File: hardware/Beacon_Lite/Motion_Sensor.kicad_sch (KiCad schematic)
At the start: 2 parts, among them U6 BMA530

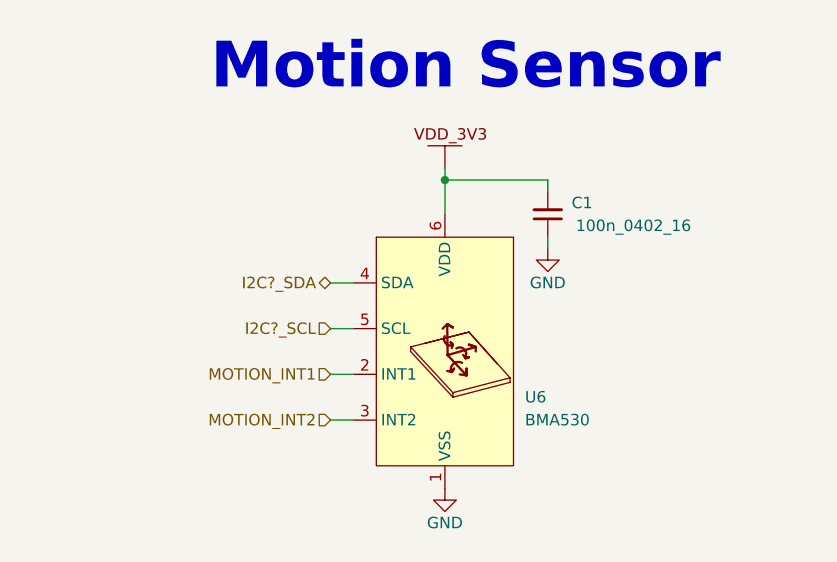
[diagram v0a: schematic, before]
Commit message: Started ST project. Create sch symbols.
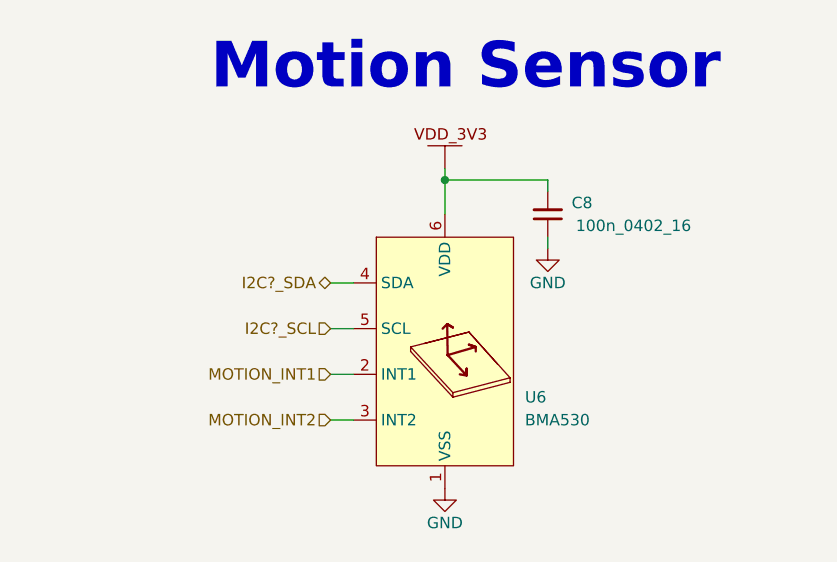
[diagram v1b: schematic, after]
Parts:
- renumbered C1 to C8

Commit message: Minor schematic and symbol updates
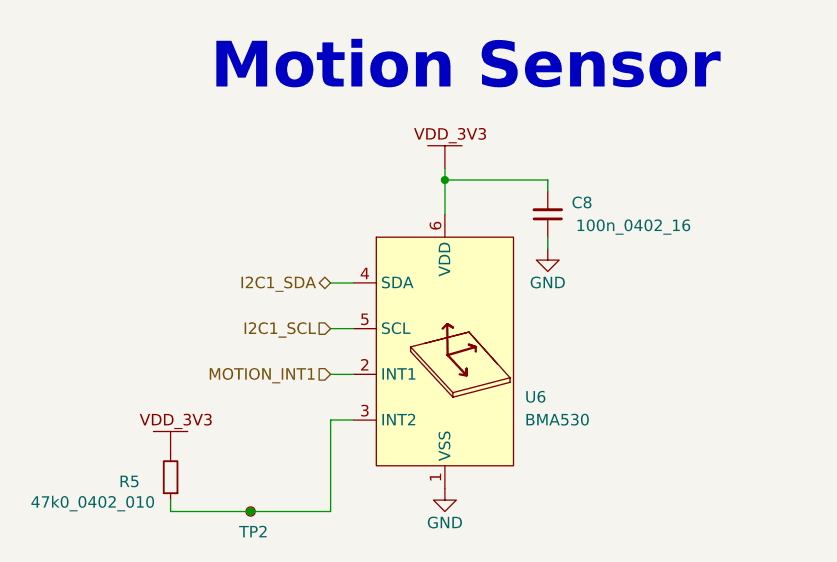
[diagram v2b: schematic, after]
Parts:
- added R5: 47k0_0402_010, Footprint_Library:0402_1005Metric_Handsolder, symbol Device:R_Small
- added TP2: TestPoint_Small, symbol Connector:TestPoint_Small
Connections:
- net VDD_3V3: now also R5.2
- net I2C?_SCL renamed I2C1_SCL
- net I2C?_SDA renamed I2C1_SDA
- net MOTION_INT2: no longer names the net of U6.3 (INT2)
- net MOTION_INT2: now also R5.1, TP2.1
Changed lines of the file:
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@@
 		(color 0 0 0 0)
 	)
+	(junction
+		(at 106.68 104.14)
+		(diameter 0)
+		(color 0 0 0 0)
+	)
+	(wire
+		(pts
+			(xy 115.57 93.98) (xy 115.57 104.14)
+		)
+		(stroke
+			(width 0)
+			(type default)
+		)
+	)
 	(wire
 		(pts
@@
 	(wire
 		(pts
+			(xy 97.79 104.14) (xy 106.68 104.14)
+		)
+		(stroke
+			(width 0)
+			(type default)
+		)
+	)
+	(wire
+		(pts
 			(xy 115.57 88.9) (xy 118.11 88.9)
 		)
@@
 	(wire
 		(pts
+			(xy 97.79 102.87) (xy 97.79 104.14)
+		)
+		(stroke
+			(width 0)
+			(type default)
+		)
+	)
+	(wire
+		(pts
 			(xy 115.57 83.82) (xy 118.11 83.82)
 		)
@@
 	(wire
 		(pts
+			(xy 115.57 104.14) (xy 106.68 104.14)
+		)
+		(stroke
+			(width 0)
+			(type default)
+		)
+	)
+	(wire
+		(pts
 			(xy 128.27 67.31) (xy 128.27 71.12)
 		)
@@
 		)
 	)
-	(hierarchical_label "I2C?_SCL"
+	(hierarchical_label "I2C1_SCL"
 		(shape input)
 		(at 115.57 83.82 180)
@@
 		)
 		(property "Intersheetrefs" "${INTERSHEET_REFS}"
-			(at 104.7786 83.82 0)
+			(at 104.5783 83.82 0)
 			(effects
 				(font
@@
 		)
 	)
-	(hierarchical_label "I2C?_SDA"
+	(hierarchical_label "I2C1_SDA"
 		(shape bidirectional)
 		(at 115.57 78.74 180)
@@
 		)
 		(property "Intersheetrefs" "${INTERSHEET_REFS}"
-			(at 104.7181 78.74 0)
-			(effects
-				(font
-					(size 1.27 1.27)
-				)
-				(justify right)
-				(hide yes)
-			)
-		)
-	)
-	(hierarchical_label "MOTION_INT2"
-		(shape input)
-		(at 115.57 93.98 180)
-		(fields_autoplaced yes)
-		(effects
-			(font
-				(size 1.27 1.27)
-			)
-			(justify right)
-		)
-		(property "Intersheetrefs" "${INTERSHEET_REFS}"
-			(at 101.3314 93.98 0)
+			(at 104.5178 78.74 0)
 			(effects
 				(font
@@
 	)
 	(symbol
+		(lib_id "Beacon_Lite_Library:VDD_3V3")
+		(at 97.79 97.79 0)
+		(unit 1)
+		(exclude_from_sim no)
+		(in_bom yes)
+		(on_board yes)
+		(dnp no)
+		(fields_autoplaced yes)
+		(property "Reference" "#PWR33"
+			(at 100.965 96.52 0)
+			(effects
+				(font
+					(size 1.27 1.27)
+				)
+				(hide yes)
+			)
+		)
+		(property "Value" "~"
+			(at 97.79 97.79 0)
+			(effects
+				(font
+					(size 1.27 1.27)
+				)
+			)
+		)
+		(property "Footprint" ""
+			(at 97.79 97.79 0)
+			(effects
+				(font
+					(size 1.27 1.27)
+				)
+				(hide yes)
+			)
+		)
+		(property "Datasheet" ""
+			(at 97.79 97.79 0)
+			(effects
+				(font
+					(size 1.27 1.27)
+				)
+				(hide yes)
+			)
+		)
+		(property "Description" ""
+			(at 97.79 97.79 0)
+			(effects
+				(font
+					(size 1.27 1.27)
+				)
+			)
+		)
+		(pin ""
+		)
+		(instances
+			(project "Beacon_Lite"
+				(path "/33ebacd6-2d94-4d95-bf8a-b8a1895869c6/961e3fea-21d0-4d6b-b514-e7b612491dfd"
+					(reference "#PWR33")
+					(unit 1)
+				)
+			)
+		)
+	)
+	(symbol
+		(lib_id "Device:R_Small")
+		(at 97.79 100.33 180)
+		(unit 1)
+		(exclude_from_sim no)
+		(in_bom yes)
+		(on_board yes)
+		(dnp no)
+		(property "Reference" "R5"
+			(at 93.218 100.838 0)
+			(effects
+				(font
+					(size 1.27 1.27)
+				)
+			)
+		)
+		(property "Value" "47k0_0402_010"
+			(at 89.154 103.124 0)
+			(effects
+				(font
+					(size 1.27 1.27)
+				)
+			)
+		)
+		(property "Footprint" "Footprint_Library:0402_1005Metric_Handsolder"
+			(at 97.79 100.33 0)
+			(effects
+				(font
+					(size 1.27 1.27)
+				)
+				(hide yes)
+			)
+		)
+		(property "Datasheet" "~"
+			(at 97.79 100.33 0)
+			(effects
+				(font
+					(size 1.27 1.27)
+				)
+				(hide yes)
+			)
+		)
+		(property "Description" ""
+			(at 97.79 100.33 0)
+			(effects
+				(font
+					(size 1.27 1.27)
+				)
+			)
+		)
+		(pin "1"
+		)
+		(pin "2"
+		)
+		(instances
+			(project "Beacon_Lite"
+				(path "/33ebacd6-2d94-4d95-bf8a-b8a1895869c6/961e3fea-21d0-4d6b-b514-e7b612491dfd"
+					(reference "R5")
+					(unit 1)
+				)
+			)
+		)
+	)
+	(symbol
 		(lib_id "Device:C_Small")
 		(at 139.7 71.12 180)
@@
 					(unit 1)
 				)
+			)
+		)
+	)
+	(symbol
+		(lib_id "Connector:TestPoint_Small")
+		(at 106.68 104.14 0)
+		(unit 1)
+		(exclude_from_sim no)
+		(in_bom yes)
+		(on_board yes)
+		(dnp no)
+		(property "Reference" "TP2"
+			(at 105.41 106.426 0)
+			(effects
+				(font
+					(size 1.27 1.27)
+				)
+				(justify left)
+			)
+		)
+		(property "Value" "TestPoint_Small"
+			(at 107.95 105.4099 0)
+			(effects
+				(font
+					(size 1.27 1.27)
+				)
+				(justify left)
+				(hide yes)
+			)
+		)
+		(property "Footprint" ""
+			(at 111.76 104.14 0)
+			(effects
+				(font
+					(size 1.27 1.27)
+				)
+				(hide yes)
+			)
+		)
+		(property "Datasheet" "~"
+			(at 111.76 104.14 0)
+			(effects
+				(font
+					(size 1.27 1.27)
+				)
+				(hide yes)
+			)
+		)
+		(property "Description" "test point"
+			(at 106.68 104.14 0)
+			(effects
+				(font
+					(size 1.27 1.27)
+				)
+				(hide yes)
+			)
+		)
+		(pin "1"
+		)
+		(instances
+			(project ""
+				(path "/33ebacd6-2d94-4d95-bf8a-b8a1895869c6/961e3fea-21d0-4d6b-b514-e7b612491dfd"
+					(reference "TP2")
+					(unit 1)
+				)
